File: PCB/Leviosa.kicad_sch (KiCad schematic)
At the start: 77 parts, among them J1 Barrel_Jack, J2 Conn_01x05_Socket, J3 2.54mm 1x03 Spare, Q1 NCE0110K, U1 SS495A, U2 LM321, U3 TPS1H200AQDGNRQ1, U4 LM393, U5 L78L10_SOT89, U6 MX27517, U7 AZ1117CH2-3.3, U8 INA199A3DCKR, U9 STM32G030F6Px

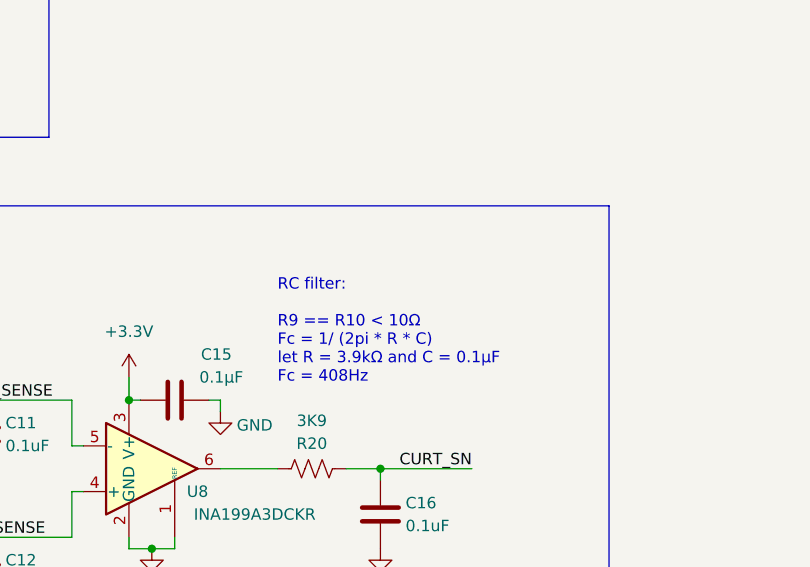
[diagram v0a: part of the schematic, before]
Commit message: CHORE: datasheets
Update datasheets to store locally and reference local datasheet
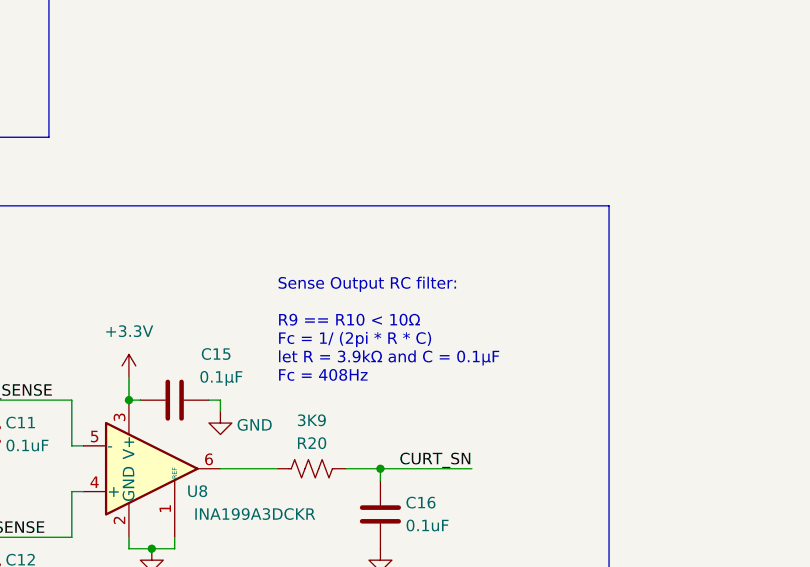
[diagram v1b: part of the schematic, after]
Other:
- note added: "Sense Output RC filter: R9 == R10 < 10Ω Fc = 1/ (2pi * R * C) let R = 3.9kΩ and C = 0.1μF Fc = 408Hz"
- note removed: "RC filter: R9 == R10 < 10Ω Fc = 1/ (2pi * R * C) let R = 3.9kΩ and C = 0.1μF Fc = 408Hz"

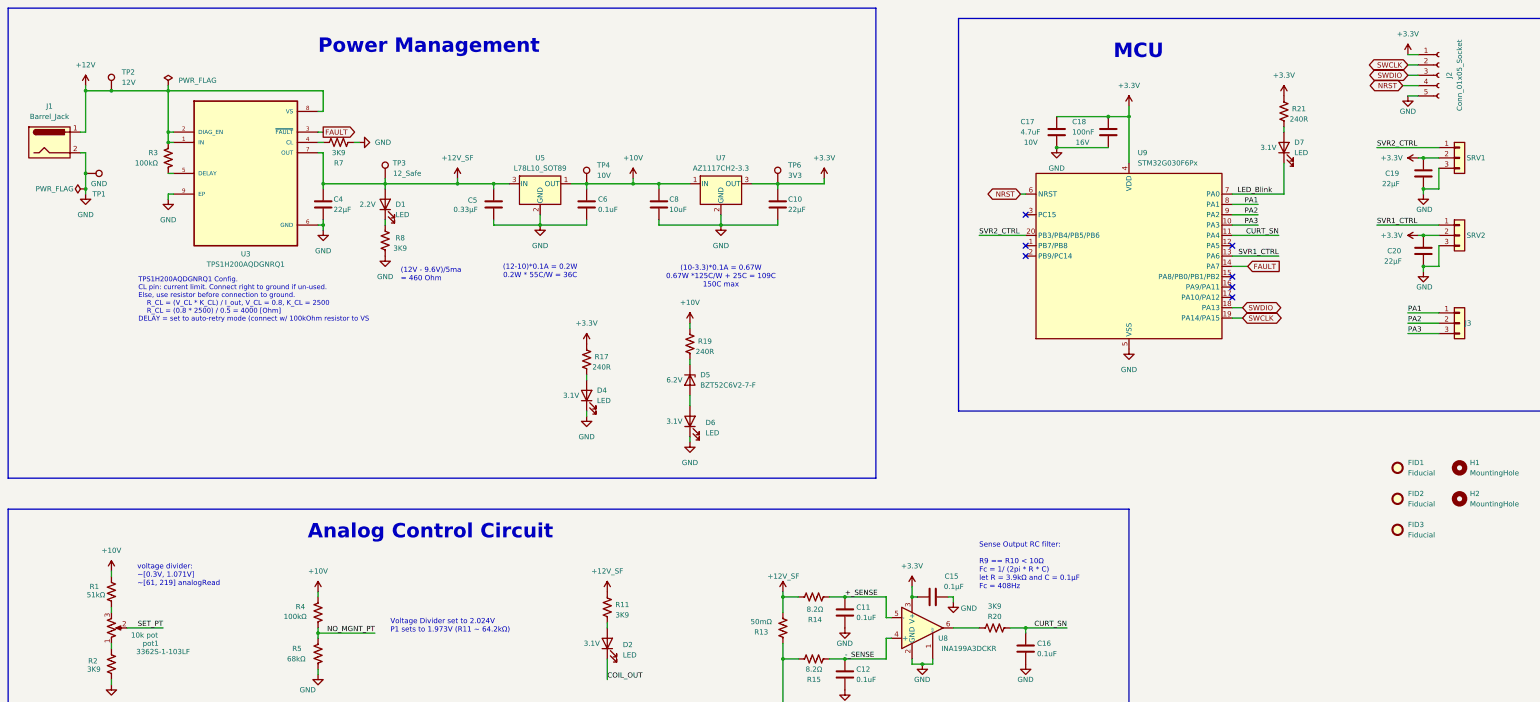
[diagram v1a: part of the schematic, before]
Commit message: CNG: update power management
1. add ESD diode on power input
2. change circuitry to allow for both 12V and 12V_SF as inputs to LDOs
3. add note about changing 3.3V LDO to a Buck instead for lower power draw
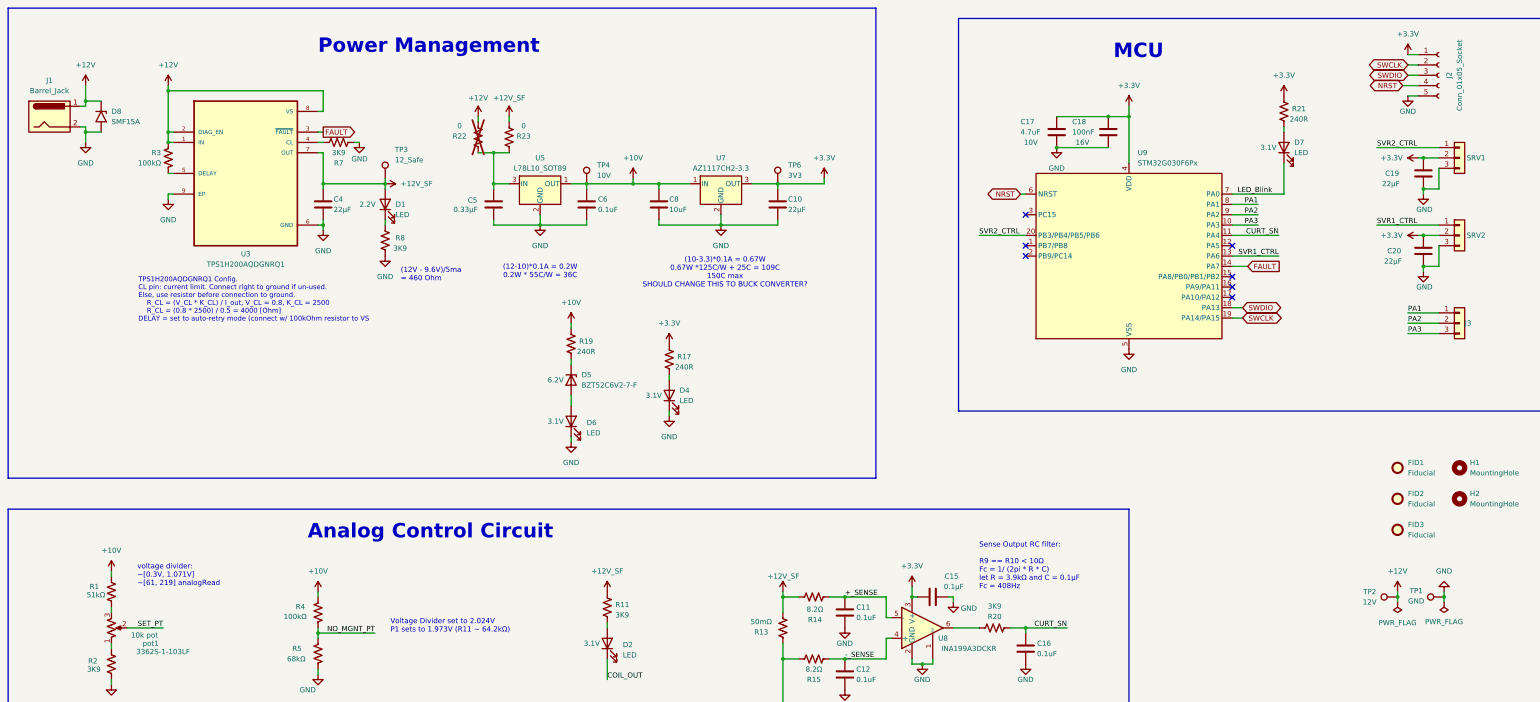
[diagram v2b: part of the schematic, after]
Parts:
- added D8: SMF15A, Diode_SMD:D_SMF, symbol Diode:SMF15A
- added R22, R23: 0, Resistor_SMD:R_0603_1608Metric, symbol Device:R_US
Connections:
- net +12V: now also D8.1 (A1), R22.1
- net +12V_SF: now also R23.1; no longer C5.1, U5.3 (IN)
- net GND: now also D8.2 (A2)
- new net: C5.1, R22.2, R23.2, U5.3 (IN)
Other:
- note added: "(10-3.3)*0.1A = 0.67W 0.67W *125C/W + 25C = 109C 150C max SHOULD CHANGE THIS TO BUCK CONVERTER?"
- note removed: "(10-3.3)*0.1A = 0.67W 0.67W *125C/W + 25C = 109C 150C max"
- moved on the sheet: D4, D5, D6, J1, R17, R19

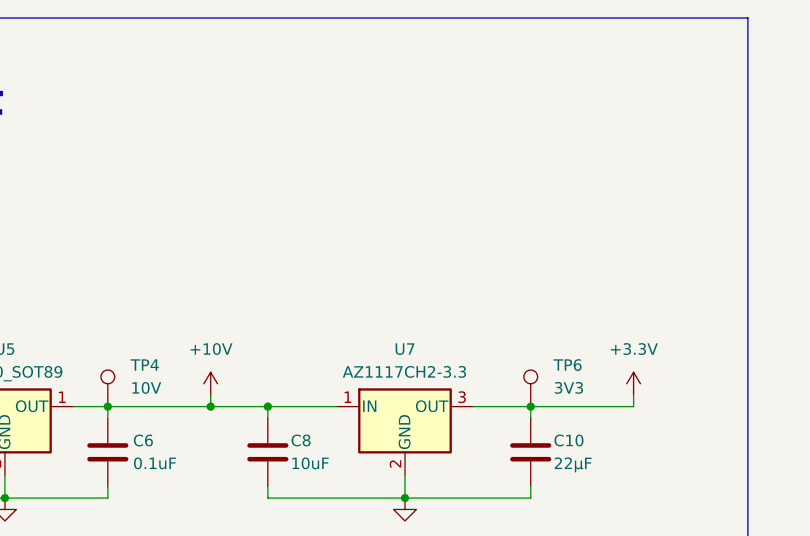
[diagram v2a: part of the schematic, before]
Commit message: CNG: 3V3 LDO to buck
Added buck converter component for 3V3 (TPS562201). Have not yet added peripheral parts or installed onto PCB
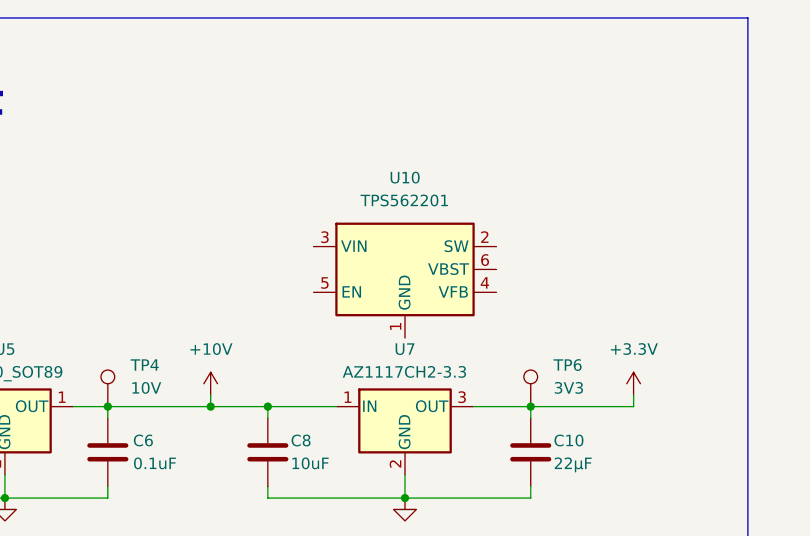
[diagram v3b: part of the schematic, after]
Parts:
- added U10: TPS562201, Package_TO_SOT_SMD:SOT-23-6, symbol Regulator_Switching:TPS562200
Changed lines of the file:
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@@
+	)
+	(symbol
+		(lib_id "Regulator_Switching:TPS562200")
+		(at 195.58 44.45 0)
+		(unit 1)
+		(body_style 1)
+		(exclude_from_sim no)
+		(in_bom yes)
+		(on_board yes)
+		(in_pos_files yes)
+		(dnp no)
+		(fields_autoplaced yes)
+		(property "Reference" "U10"
+			(at 195.58 34.29 0)
+			(show_name no)
+			(do_not_autoplace no)
+			(effects
+				(font
+					(size 1.27 1.27)
+				)
+			)
+		)
+		(property "Value" "TPS562201"
+			(at 195.58 36.83 0)
+			(show_name no)
+			(do_not_autoplace no)
+			(effects
+				(font
+					(size 1.27 1.27)
+				)
+			)
+		)
+		(property "Footprint" "Package_TO_SOT_SMD:SOT-23-6"
+			(at 196.85 50.8 0)
+			(hide yes)
+			(show_name no)
+			(do_not_autoplace no)
+			(effects
+				(font
+					(size 1.27 1.27)
+				)
+				(justify left)
+			)
+		)
+		(property "Datasheet" "file://${KIPRJMOD}/datasheets/tps562201.pdf"
+			(at 195.58 44.45 0)
+			(hide yes)
+			(show_name no)
+			(do_not_autoplace no)
+			(effects
+				(font
+					(size 1.27 1.27)
+				)
+			)
+		)
+		(property "Description" "2A Synchronous Step-Down Voltage Regulator, Adjustable Output Voltage, 4.5-17V Input Voltage, SOT-23-6"
+			(at 195.58 44.45 0)
+			(hide yes)
+			(show_name no)
+			(do_not_autoplace no)
+			(effects
+				(font
+					(size 1.27 1.27)
+				)
+			)
+		)
+		(property "Link" "https://jlcpcb.com/partdetail/TexasInstruments-TPS562201DDCR/C90061"
+			(at 195.58 44.45 0)
+			(hide yes)
+			(show_name no)
+			(do_not_autoplace no)
+			(effects
+				(font
+					(size 1.27 1.27)
+				)
+			)
+		)
+		(pin "1"
+		)
+		(pin "3"
+		)
+		(pin "5"
+		)
+		(pin "2"
+		)
+		(pin "4"
+		)
+		(pin "6"
+		)
+		(instances
+			(project "Leviosa"
+				(path "/fe766911-203b-467c-b704-d4bd488f6c98"
+					(reference "U10")
+					(unit 1)
+				)
+			)
+		)
 	)
 	(symbol

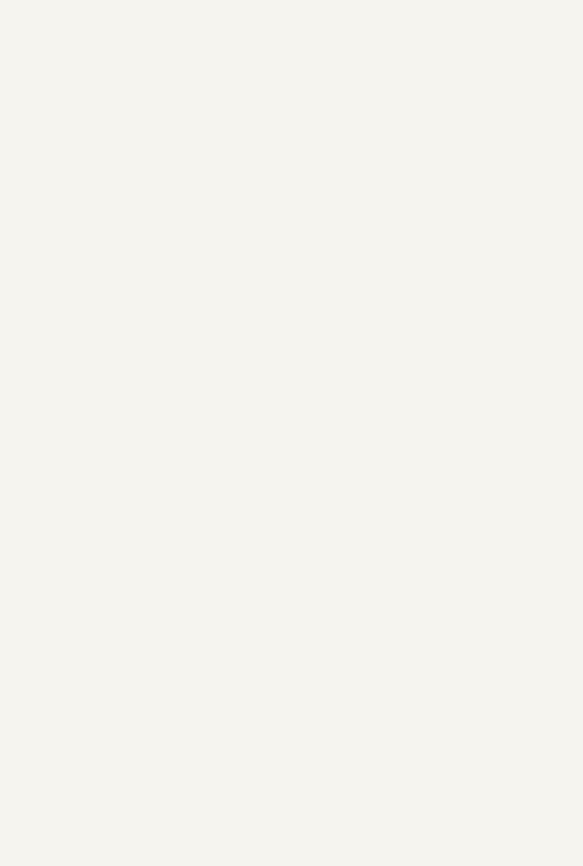
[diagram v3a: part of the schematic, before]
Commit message: NEW: TPS61088RHLR
- add component into library
- added component but have not added peripherals or other connections
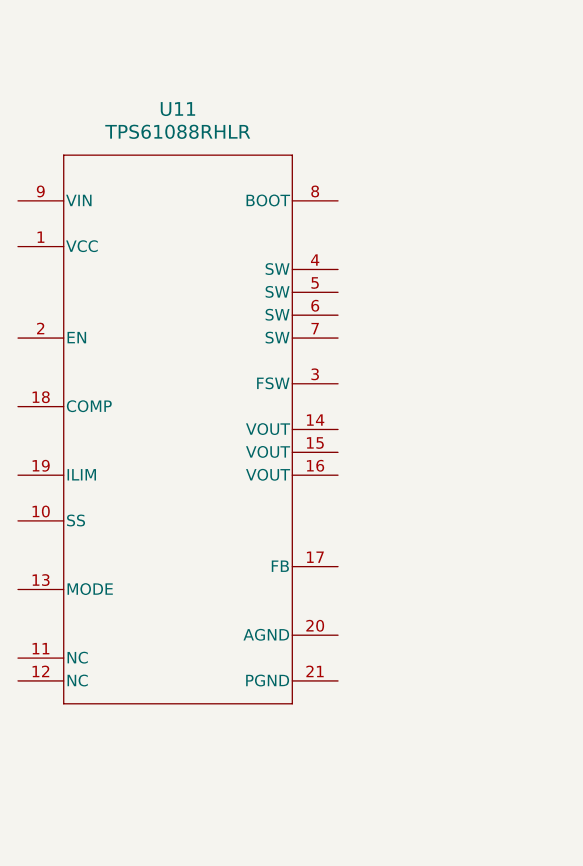
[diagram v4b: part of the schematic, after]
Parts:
- added U11: TPS61088RHLR, TPS61088:RHL0020A, symbol TPS61088:TPS61088RHLR
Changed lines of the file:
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@@
+	)
+	(symbol
+		(lib_id "TPS61088:TPS61088RHLR")
+		(at -29.21 62.23 0)
+		(unit 1)
+		(body_style 1)
+		(exclude_from_sim no)
+		(in_bom yes)
+		(on_board yes)
+		(in_pos_files yes)
+		(dnp no)
+		(fields_autoplaced yes)
+		(property "Reference" "U11"
+			(at -29.21 26.67 0)
+			(show_name no)
+			(do_not_autoplace no)
+			(effects
+				(font
+					(size 1.524 1.524)
+				)
+			)
+		)
+		(property "Value" "TPS61088RHLR"
+			(at -29.21 29.21 0)
+			(show_name no)
+			(do_not_autoplace no)
+			(effects
+				(font
+					(size 1.524 1.524)
+				)
+			)
+		)
+		(property "Footprint" "TPS61088:RHL0020A"
+			(at -29.21 62.23 0)
+			(hide yes)
+			(show_name no)
+			(do_not_autoplace no)
+			(effects
+				(font
+					(size 1.27 1.27)
+					(italic yes)
+				)
+			)
+		)
+		(property "Datasheet" "file://${KIPRJMOD}/datasheets/tps61088.pdf"
+			(at -29.21 62.23 0)
+			(hide yes)
+			(show_name no)
+			(do_not_autoplace no)
+			(effects
+				(font
+					(size 1.27 1.27)
+					(italic yes)
+				)
+			)
+		)
+		(property "Description" ""
+			(at -29.21 62.23 0)
+			(hide yes)
+			(show_name no)
+			(do_not_autoplace no)
+			(effects
+				(font
+					(size 1.27 1.27)
+				)
+			)
+		)
+		(property "Link" "https://www.lcsc.com/product-detail/C87357.html?s_z=n_q_TPS61088&spm=wm.fly.bg.0.xh&lcsc_vid=FARbA1ZeT1IPU1ZQQVZZUwdRQARbAVEHQVJXVVJXQVgxVlNeQlJZX1BUQVJdVjsOAxUeFF5JWBYZEEoKFBINSQcJGk4eFQsCAgIaSgADAwAHC0slRVZYUlVeQU8GEwkK"
+			(at -29.21 62.23 0)
+			(hide yes)
+			(show_name no)
+			(do_not_autoplace no)
+			(effects
+				(font
+					(size 1.27 1.27)
+				)
+			)
+		)
+		(pin "10"
+		)
+		(pin "2"
+		)
+		(pin "3"
+		)
+		(pin "15"
+		)
+		(pin "17"
+		)
+		(pin "18"
+		)
+		(pin "20"
+		)
+		(pin "6"
+		)
+		(pin "11"
+		)
+		(pin "19"
+		)
+		(pin "21"
+		)
+		(pin "4"
+		)
+		(pin "7"
+		)
+		(pin "9"
+		)
+		(pin "12"
+		)
+		(pin "13"
+		)
+		(pin "8"
+		)
+		(pin "5"
+		)
+		(pin "16"
+		)
+		(pin "1"
+		)
+		(pin "14"
+		)
+		(instances
+			(project "Leviosa"
+				(path "/fe766911-203b-467c-b704-d4bd488f6c98"
+					(reference "U11")
+					(unit 1)
+				)
+			)
+		)
 	)
 	(symbol
